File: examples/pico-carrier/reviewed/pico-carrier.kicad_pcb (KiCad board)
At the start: 2 copper layers, 80 x 56 mm, 9 parts, among them J1 5V IN, J3 GP0-GP15, J4 GP16-GP28, PWR, U1 Pico

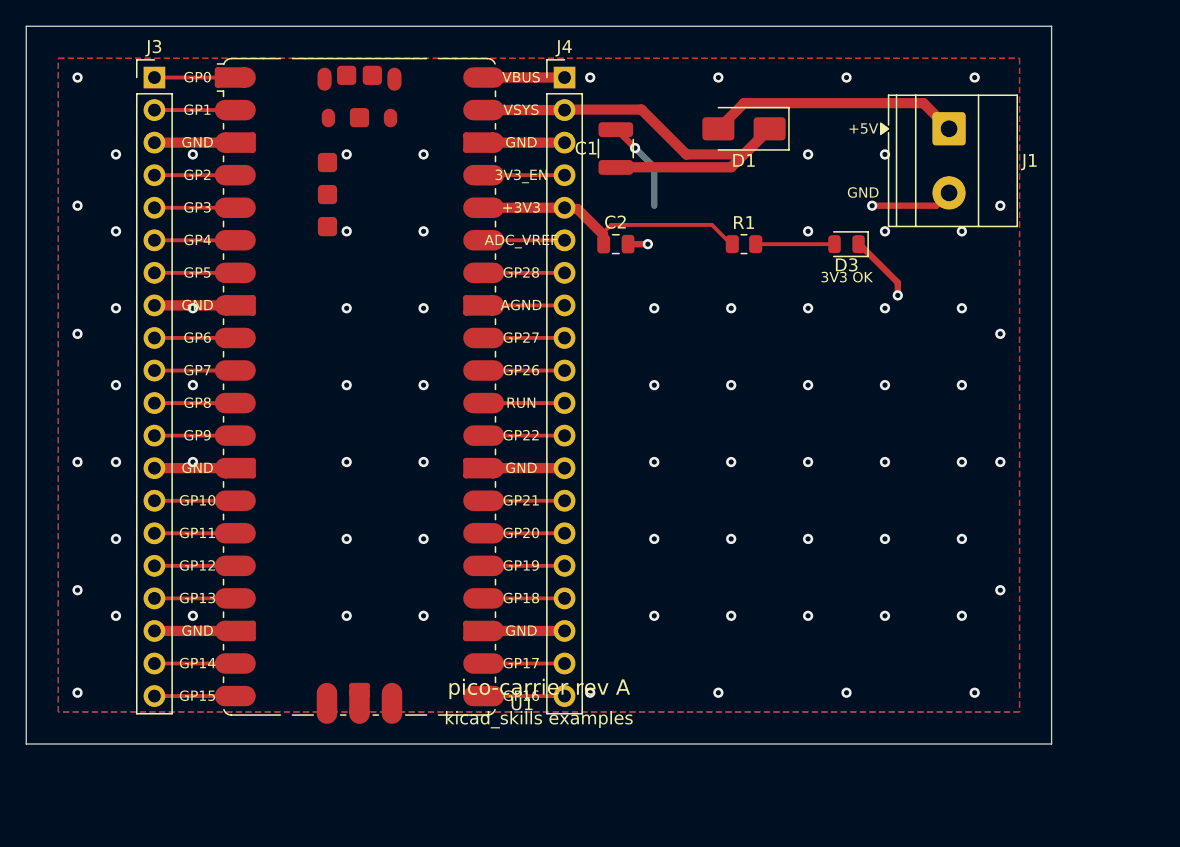
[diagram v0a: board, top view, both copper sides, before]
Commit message: Put the silkscreen where the board is not
Three legends were printed across pads. The board id was written at the
bottom centre whether or not the bottom centre was a module; the pin
names beside a connector went toward the middle of the board, which on a
carrier is the module they are labelling; and a footprint's designator
stayed where its library had drawn it, which on a part with pads down
both sides and along the bottom is the middle of a pad. Silk over a pad
is not a legend - the mask opens there, the ink comes off in
fabrication, and what is left is a pad that will not wet.

So all three ask first. The board id offers its usual spot and then the
next-best strips in turn. A pin name measures the *area* it would take
from other footprints on either side of the row and picks the smaller,
which chooses outboard on its own where there is an edge to face, and
matters because "half a legend over a module's pads" and "a tenth of a
millimetre into a chip capacitor's courtyard" are both one collision and
only one of them is a defect. A designator steps to the first spot in
its own footprint that no pad occupies.

Modules that draw no courtyard are measured by their pads instead:
taking a missing courtyard to mean the part occupies no board is how the
Pico's legend ended up across it.

The Pico carrier also grew: its two headers and the module run the
length of the board, and the plane could not get past their pin rows at
either end, so it was three islands with the return current going the
long way round. Six millimetres of board below the last pin is what a
plane needs to be one plane.
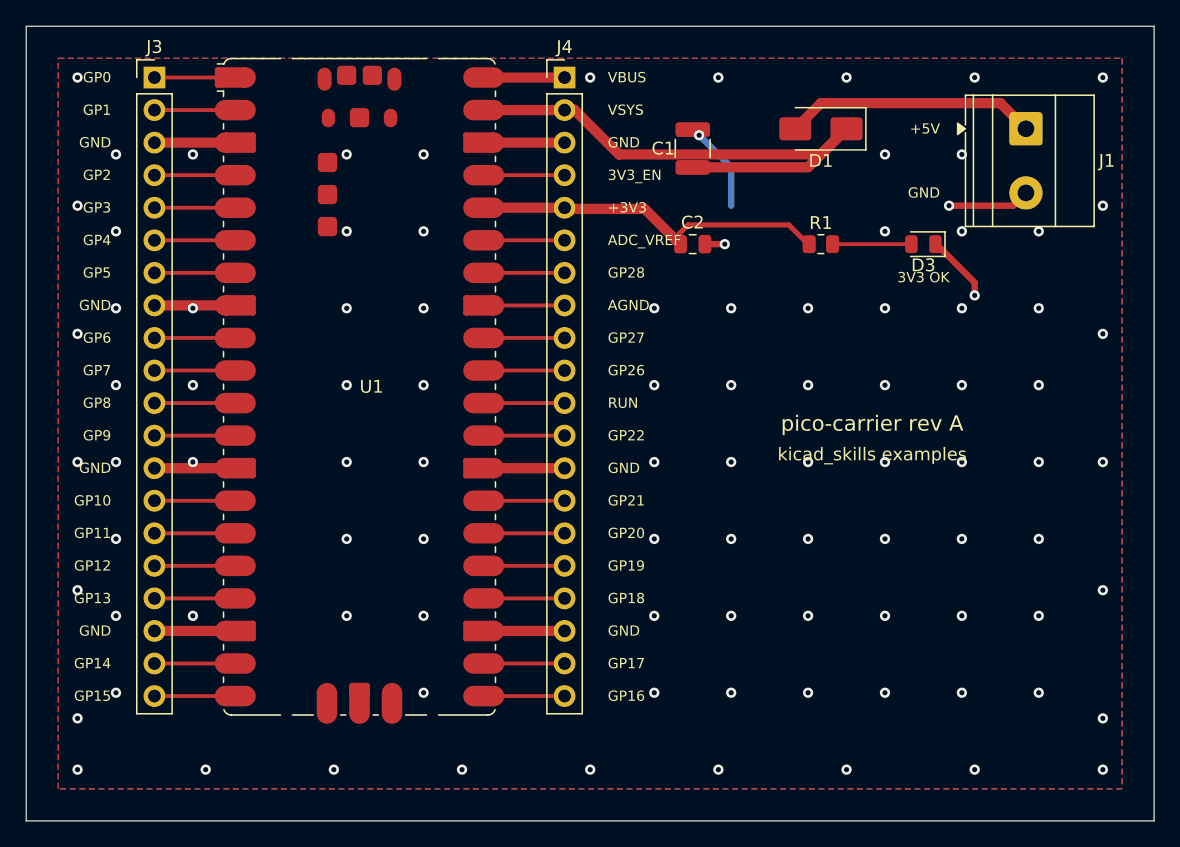
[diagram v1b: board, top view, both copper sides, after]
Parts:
- moved C1 6.00 mm to (152.0, 69.5)
- moved C2 6.00 mm to (152.0, 77.0)
- moved D1 6.00 mm to (162.0, 68.0)
- moved D3 6.00 mm to (170.0, 77.0)
- moved J1 6.00 mm to (178.0, 68.0)
- moved R1 6.00 mm to (162.0, 77.0)
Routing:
- net /VSYS: track 37.9 -> 43.9 mm
- net +3V3: track 22.8 -> 28.4 mm
- net GND: vias 78 -> 98
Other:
- board size 80 x 56 mm -> 88 x 62 mm
